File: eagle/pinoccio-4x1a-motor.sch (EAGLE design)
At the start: 27 parts, among them IC1 74LVC1G04DBV, IC2 74LVC1G04DBV, IC3 74LVC1G04DBV, IC4 74LVC1G04DBV, J1 POWER_JACKPTH, U1 TB6621FNG, U2 TB6621FNG

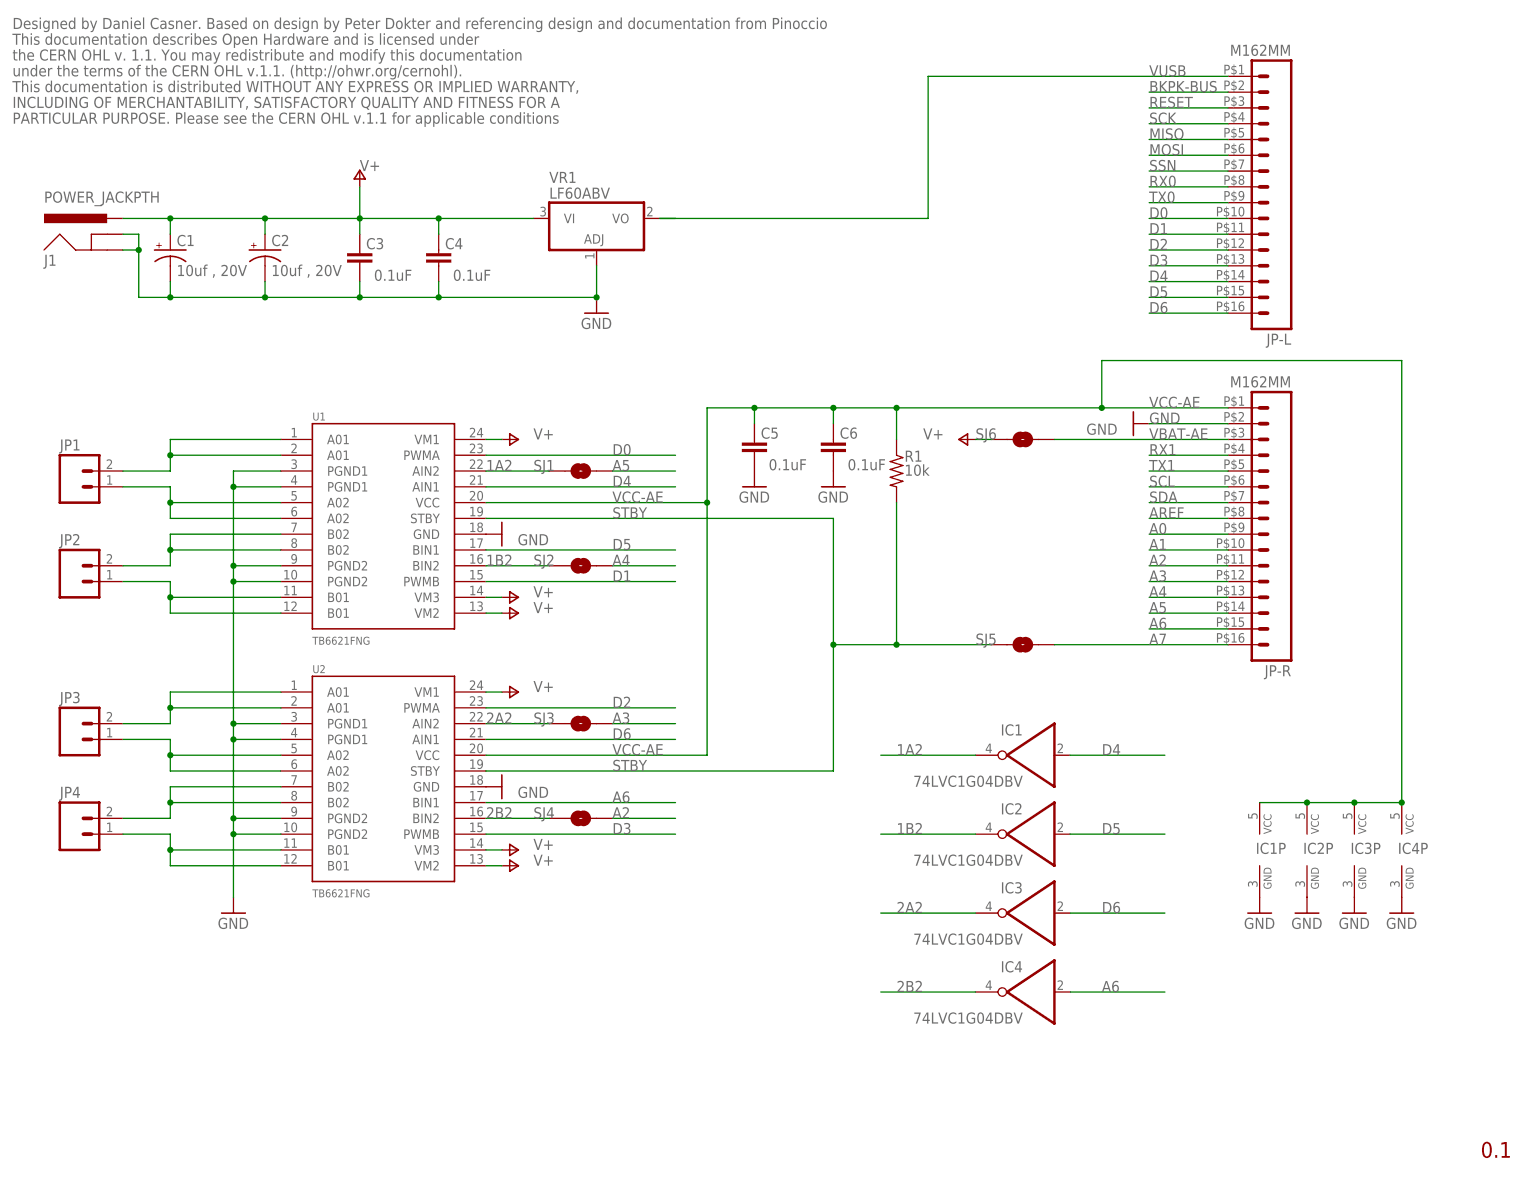
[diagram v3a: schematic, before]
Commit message: Add Atiny13 backpack ID chip. Connect LED and backpack standby to unused GPIO pins on the ATiny13.
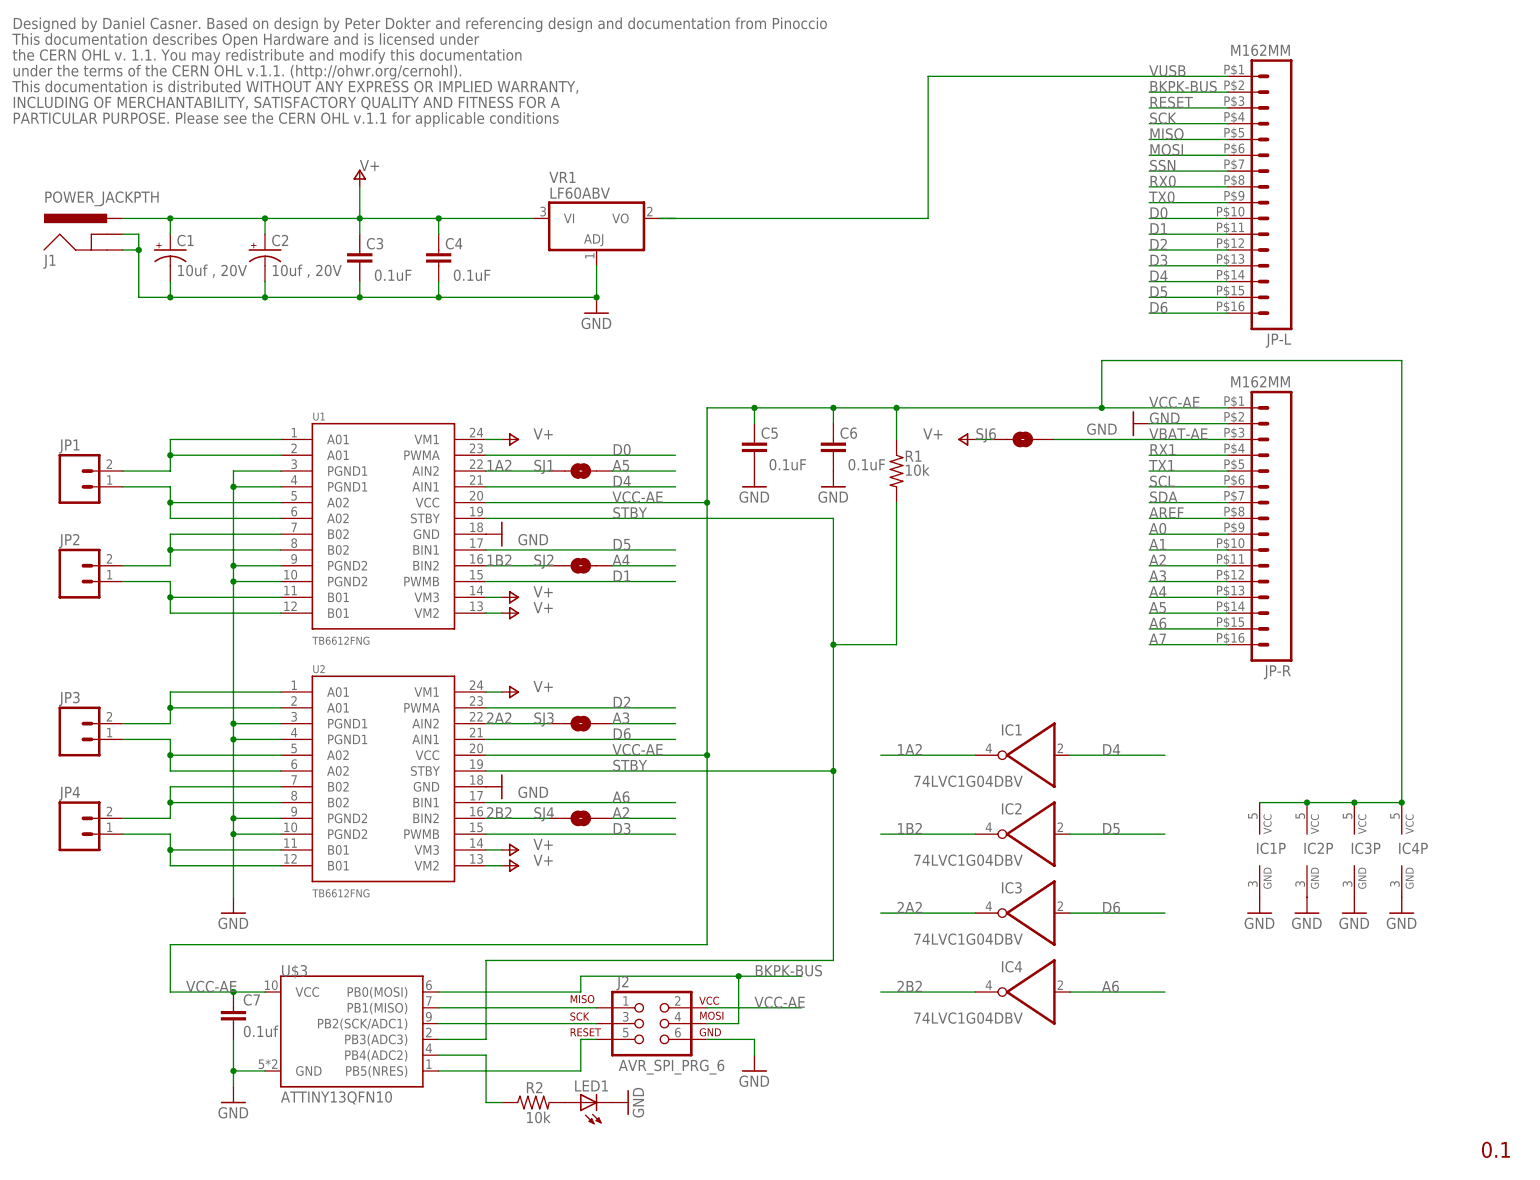
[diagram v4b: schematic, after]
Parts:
- removed SJ5: SOLDERJUMPERNC2, SparkFun-Passives:SOLDERJUMPERNC2
- added C7: 0.1uf, Pinoccio:CAP0402-CAP
- added J2: AVR_SPI_PRG_6, Pinoccio:AVR_SPI_PRG_6
- added LED1: (no value), SparkFun-LED:LED0603
- added R2: 10k, rcl:R-US_R0402
- added U$3: ATTINY13QFN10, Pinoccio:ATTINY13QFN10
- U1, U2: value TB6621FNG -> TB6612FNG
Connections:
- new net N$1: R2.1, U$3.PB4(ADC2)
- new net N$2: J2.1, U$3.PB1(MISO)
- new net N$3: J2.3, U$3.PB2(SCK/ADC1)
- new net N$4: J2.5, U$3.PB5(NRES)
- new net N$5: LED1.A, R2.2
- net A7: no longer SJ5.2
- net BKPK-BUS: now also J2.4, U$3.PB0(MOSI)
- net GND: now also C7.2, J2.6, LED1.C, U$3.GND
- net STBY: now also U$3.PB3(ADC3); no longer SJ5.1
- net VCC-AE: now also C7.1, J2.2, U$3.VCC
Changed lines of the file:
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@@
 <part name="JP-R" library="Pinoccio" deviceset="M16" device="2MM"/>
 <part name="JP-L" library="Pinoccio" deviceset="M16" device="2MM"/>
-<part name="U1" library="SparkFun" deviceset="TB6621FNG" device=""/>
-<part name="U2" library="SparkFun" deviceset="TB6621FNG" device=""/>
+<part name="U1" library="SparkFun" deviceset="TB6621FNG" device="" value="TB6612FNG"/>
+<part name="U2" library="SparkFun" deviceset="TB6621FNG" device="" value="TB6612FNG"/>
 <part name="VR1" library="linear" deviceset="*317" device="T" value="LF60ABV"/>
 <part name="C3" library="SparkFun" deviceset="CAP" device="0402-CAP" value="0.1uF"/>
@@
 <part name="P+7" library="supply1" deviceset="V+" device=""/>
 <part name="R1" library="rcl" deviceset="R-US_" device="R0402" value="10k"/>
-<part name="SJ5" library="SparkFun-Passives" deviceset="SOLDERJUMPER" device="NC2"/>
 <part name="SJ6" library="SparkFun-Passives" deviceset="SOLDERJUMPER" device="NC2"/>
 <part name="P+8" library="supply1" deviceset="V+" device=""/>
@@
 <part name="GND11" library="SparkFun-Aesthetics" deviceset="GND" device=""/>
 <part name="GND12" library="SparkFun-Aesthetics" deviceset="GND" device=""/>
+<part name="U$3" library="Pinoccio" deviceset="ATTINY13" device="QFN10"/>
+<part name="J2" library="Pinoccio" deviceset="AVR_SPI_PRG_6" device=""/>
+<part name="C7" library="Pinoccio" deviceset="CAP" device="0402-CAP" value="0.1uf"/>
+<part name="GND2" library="SparkFun-Aesthetics" deviceset="GND" device=""/>
+<part name="GND13" library="SparkFun-Aesthetics" deviceset="GND" device=""/>
+<part name="R2" library="rcl" deviceset="R-US_" device="R0402" value="10k"/>
+<part name="LED1" library="SparkFun-LED" deviceset="LED" device="0603"/>
+<part name="GND14" library="SparkFun-Aesthetics" deviceset="GND" device=""/>
 </parts>
 <sheets>
@@
 <attribute name="VALUE" x="146.05" y="110.998" size="1.778" layer="96"/>
 </instance>
-<instance part="SJ5" gate="1" x="165.1" y="83.82" smashed="yes">
-<attribute name="NAME" x="157.48" y="83.82" size="1.778" layer="95"/>
-</instance>
 <instance part="SJ6" gate="1" x="165.1" y="116.84" smashed="yes">
 <attribute name="NAME" x="157.48" y="116.84" size="1.778" layer="95"/>
@@
 <instance part="GND11" gate="1" x="134.62" y="109.22"/>
 <instance part="GND12" gate="1" x="121.92" y="109.22"/>
+<instance part="U$3" gate="G$1" x="58.42" y="20.32"/>
+<instance part="J2" gate="G$1" x="104.14" y="22.86"/>
+<instance part="C7" gate="G$1" x="38.1" y="22.86"/>
+<instance part="GND2" gate="1" x="38.1" y="10.16"/>
+<instance part="GND13" gate="1" x="121.92" y="15.24"/>
+<instance part="R2" gate="G$1" x="86.36" y="10.16" smashed="yes">
+<attribute name="NAME" x="85.09" y="11.6586" size="1.778" layer="95"/>
+<attribute name="VALUE" x="85.09" y="6.858" size="1.778" layer="96"/>
+</instance>
+<instance part="LED1" gate="G$1" x="93.98" y="10.16" rot="R90"/>
+<instance part="GND14" gate="1" x="101.6" y="10.16" rot="R90"/>
 </instances>
 <busses>
@@
 <pinref part="GND12" gate="1" pin="GND"/>
 </segment>
+<segment>
+<pinref part="U$3" gate="G$1" pin="GND"/>
+<wire x1="43.18" y1="15.24" x2="38.1" y2="15.24" width="0.1524" layer="91"/>
+<wire x1="38.1" y1="15.24" x2="38.1" y2="12.7" width="0.1524" layer="91"/>
+<pinref part="C7" gate="G$1" pin="2"/>
+<wire x1="38.1" y1="20.32" x2="38.1" y2="15.24" width="0.1524" layer="91"/>
+<junction x="38.1" y="15.24"/>
+<pinref part="GND2" gate="1" pin="GND"/>
+</segment>
+<segment>
+<pinref part="J2" gate="G$1" pin="6"/>
+<wire x1="114.3" y1="20.32" x2="121.92" y2="20.32" width="0.1524" layer="91"/>
+<wire x1="121.92" y1="20.32" x2="121.92" y2="17.78" width="0.1524" layer="91"/>
+<pinref part="GND13" gate="1" pin="GND"/>
+</segment>
+<segment>
+<pinref part="LED1" gate="G$1" pin="C"/>
+<pinref part="GND14" gate="1" pin="GND"/>
+</segment>
 </net>
 <net name="MOSI" class="0">
@@
 </segment>
 </net>
-<net name="A7" class="0">
-<segment>
-<pinref part="JP-R" gate="G$1" pin="16"/>
-<label x="185.42" y="83.82" size="1.778" layer="95"/>
-<wire x1="198.12" y1="83.82" x2="170.18" y2="83.82" width="0.1524" layer="91"/>
-<pinref part="SJ5" gate="1" pin="2"/>
-</segment>
-</net>
 <net name="VCC-AE" class="0">
 <segment>
@@
 <junction x="134.62" y="121.92"/>
 <junction x="121.92" y="121.92"/>
+<wire x1="114.3" y1="66.04" x2="114.3" y2="35.56" width="0.1524" layer="91"/>
+<pinref part="U$3" gate="G$1" pin="VCC"/>
+<wire x1="43.18" y1="27.94" x2="38.1" y2="27.94" width="0.1524" layer="91"/>
+<label x="30.48" y="27.94" size="1.778" layer="95"/>
+<pinref part="C7" gate="G$1" pin="1"/>
+<wire x1="38.1" y1="27.94" x2="27.94" y2="27.94" width="0.1524" layer="91"/>
+<junction x="38.1" y="27.94"/>
+<wire x1="114.3" y1="35.56" x2="27.94" y2="35.56" width="0.1524" layer="91"/>
+<wire x1="27.94" y1="35.56" x2="27.94" y2="27.94" width="0.1524" layer="91"/>
+<junction x="114.3" y="66.04"/>
+</segment>
+<segment>
+<pinref part="J2" gate="G$1" pin="2"/>
+<wire x1="114.3" y1="25.4" x2="129.54" y2="25.4" width="0.1524" layer="91"/>
+<label x="121.92" y="25.4" size="1.778" layer="95"/>
 </segment>
 </net>
@@
 <label x="99.06" y="104.14" size="1.778" layer="95"/>
 <pinref part="R1" gate="G$1" pin="2"/>
-<pinref part="SJ5" gate="1" pin="1"/>
 <wire x1="144.78" y1="106.68" x2="144.78" y2="83.82" width="0.1524" layer="91"/>
-<wire x1="144.78" y1="83.82" x2="160.02" y2="83.82" width="0.1524" layer="91"/>
 <wire x1="144.78" y1="83.82" x2="134.62" y2="83.82" width="0.1524" layer="91"/>
 <wire x1="134.62" y1="104.14" x2="134.62" y2="83.82" width="0.1524" layer="91"/>
@@
 <wire x1="134.62" y1="83.82" x2="134.62" y2="63.5" width="0.1524" layer="91"/>
 <junction x="134.62" y="83.82"/>
-<junction x="144.78" y="83.82"/>
+<wire x1="78.74" y1="33.02" x2="134.62" y2="33.02" width="0.1524" layer="91"/>
+<wire x1="134.62" y1="33.02" x2="134.62" y2="63.5" width="0.1524" layer="91"/>
+<junction x="134.62" y="63.5"/>
+<wire x1="78.74" y1="33.02" x2="78.74" y2="20.32" width="0.1524" layer="91"/>
+<pinref part="U$3" gate="G$1" pin="PB3(ADC3)"/>
+<wire x1="78.74" y1="20.32" x2="71.12" y2="20.32" width="0.1524" layer="91"/>
 </segment>
 </net>
@@
 <wire x1="198.12" y1="172.72" x2="185.42" y2="172.72" width="0.1524" layer="91"/>
 </segment>
+<segment>
+<pinref part="J2" gate="G$1" pin="4"/>
+<wire x1="114.3" y1="22.86" x2="119.38" y2="22.86" width="0.1524" layer="91"/>
+<wire x1="119.38" y1="22.86" x2="119.38" y2="30.48" width="0.1524" layer="91"/>
+<pinref part="U$3" gate="G$1" pin="PB0(MOSI)"/>
+<wire x1="119.38" y1="30.48" x2="93.98" y2="30.48" width="0.1524" layer="91"/>
+<wire x1="93.98" y1="30.48" x2="93.98" y2="27.94" width="0.1524" layer="91"/>
+<wire x1="93.98" y1="27.94" x2="71.12" y2="27.94" width="0.1524" layer="91"/>
+<wire x1="119.38" y1="30.48" x2="129.54" y2="30.48" width="0.1524" layer="91"/>
+<junction x="119.38" y="30.48"/>
+<label x="121.92" y="30.48" size="1.778" layer="95"/>
+</segment>
+</net>
+<net name="N$3" class="0">
+<segment>
+<pinref part="J2" gate="G$1" pin="3"/>
+<pinref part="U$3" gate="G$1" pin="PB2(SCK/ADC1)"/>
+<wire x1="96.52" y1="22.86" x2="71.12" y2="22.86" width="0.1524" layer="91"/>
+</segment>
+</net>
+<net name="N$4" class="0">
+<segment>
+<pinref part="J2" gate="G$1" pin="5"/>
+<wire x1="96.52" y1="20.32" x2="93.98" y2="20.32" width="0.1524" layer="91"/>
+<wire x1="93.98" y1="20.32" x2="93.98" y2="15.24" width="0.1524" layer="91"/>
+<pinref part="U$3" gate="G$1" pin="PB5(NRES)"/>
+<wire x1="93.98" y1="15.24" x2="71.12" y2="15.24" width="0.1524" layer="91"/>
+</segment>
+</net>
+<net name="A7" class="0">
+<segment>
+<pinref part="JP-R" gate="G$1" pin="16"/>
+<wire x1="198.12" y1="83.82" x2="185.42" y2="83.82" width="0.1524" layer="91"/>
+<label x="185.42" y="83.82" size="1.778" layer="95"/>
+</segment>
+</net>
+<net name="N$1" class="0">
+<segment>
+<pinref part="U$3" gate="G$1" pin="PB4(ADC2)"/>
+<pinref part="R2" gate="G$1" pin="1"/>
+<wire x1="81.28" y1="10.16" x2="78.74" y2="10.16" width="0.1524" layer="91"/>
+<wire x1="78.74" y1="10.16" x2="78.74" y2="17.78" width="0.1524" layer="91"/>
+<wire x1="78.74" y1="17.78" x2="71.12" y2="17.78" width="0.1524" layer="91"/>
+</segment>
+</net>
+<net name="N$2" class="0">
+<segment>
+<pinref part="U$3" gate="G$1" pin="PB1(MISO)"/>
+<pinref part="J2" gate="G$1" pin="1"/>
+<wire x1="96.52" y1="25.4" x2="71.12" y2="25.4" width="0.1524" layer="91"/>
+</segment>
+</net>
+<net name="N$5" class="0">
+<segment>
+<pinref part="R2" gate="G$1" pin="2"/>
+<pinref part="LED1" gate="G$1" pin="A"/>
+</segment>
 </net>

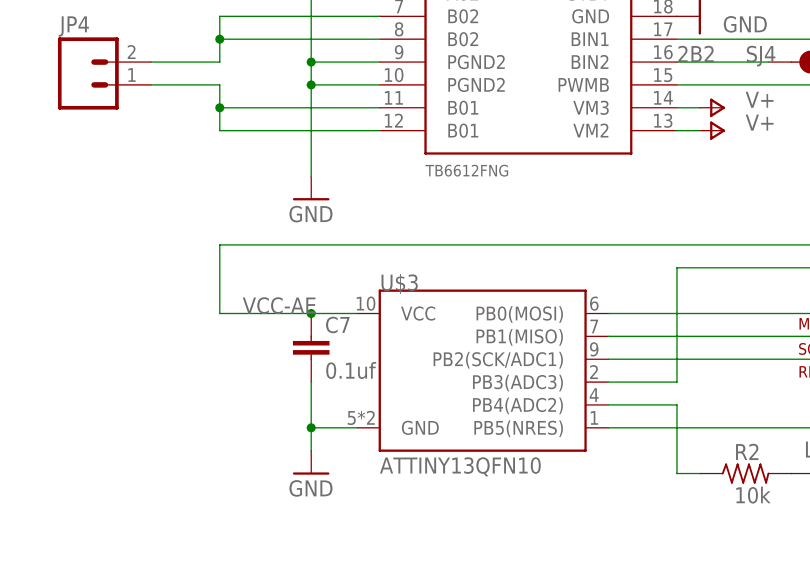
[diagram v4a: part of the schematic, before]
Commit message: Tru ripping up all the autorouted signals before rerouting.
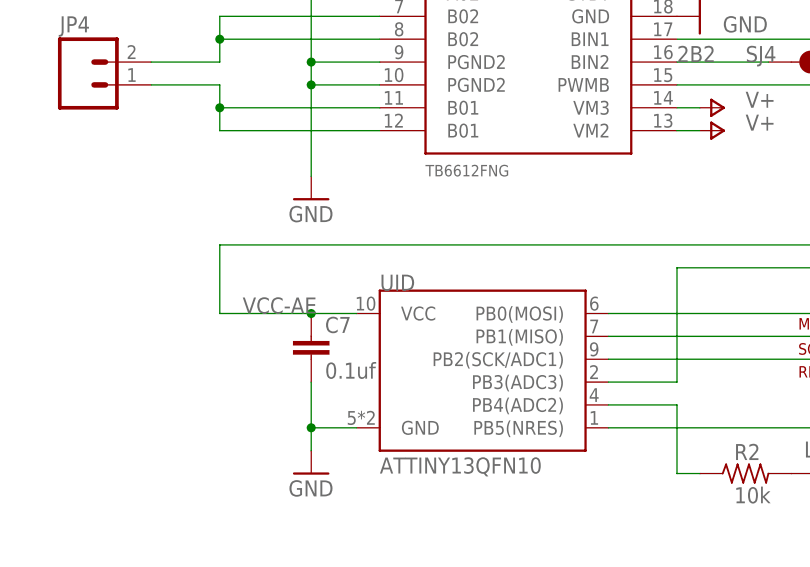
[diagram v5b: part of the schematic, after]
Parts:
- renumbered U$3 to UID
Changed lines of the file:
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@@
 <part name="GND11" library="SparkFun-Aesthetics" deviceset="GND" device=""/>
 <part name="GND12" library="SparkFun-Aesthetics" deviceset="GND" device=""/>
-<part name="U$3" library="Pinoccio" deviceset="ATTINY13" device="QFN10"/>
+<part name="UID" library="Pinoccio" deviceset="ATTINY13" device="QFN10"/>
 <part name="J2" library="Pinoccio" deviceset="AVR_SPI_PRG_6" device=""/>
 <part name="C7" library="Pinoccio" deviceset="CAP" device="0402-CAP" value="0.1uf"/>
@@
 <instance part="GND11" gate="1" x="134.62" y="109.22"/>
 <instance part="GND12" gate="1" x="121.92" y="109.22"/>
-<instance part="U$3" gate="G$1" x="58.42" y="20.32"/>
+<instance part="UID" gate="G$1" x="58.42" y="20.32"/>
 <instance part="J2" gate="G$1" x="104.14" y="22.86"/>
 <instance part="C7" gate="G$1" x="38.1" y="22.86"/>
@@
 </segment>
 <segment>
-<pinref part="U$3" gate="G$1" pin="GND"/>
+<pinref part="UID" gate="G$1" pin="GND"/>
 <wire x1="43.18" y1="15.24" x2="38.1" y2="15.24" width="0.1524" layer="91"/>
 <wire x1="38.1" y1="15.24" x2="38.1" y2="12.7" width="0.1524" layer="91"/>
@@
 <junction x="121.92" y="121.92"/>
 <wire x1="114.3" y1="66.04" x2="114.3" y2="35.56" width="0.1524" layer="91"/>
-<pinref part="U$3" gate="G$1" pin="VCC"/>
+<pinref part="UID" gate="G$1" pin="VCC"/>
 <wire x1="43.18" y1="27.94" x2="38.1" y2="27.94" width="0.1524" layer="91"/>
 <label x="30.48" y="27.94" size="1.778" layer="95"/>
@@
 <junction x="134.62" y="63.5"/>
 <wire x1="78.74" y1="33.02" x2="78.74" y2="20.32" width="0.1524" layer="91"/>
-<pinref part="U$3" gate="G$1" pin="PB3(ADC3)"/>
+<pinref part="UID" gate="G$1" pin="PB3(ADC3)"/>
 <wire x1="78.74" y1="20.32" x2="71.12" y2="20.32" width="0.1524" layer="91"/>
 </segment>
@@
 <wire x1="114.3" y1="22.86" x2="119.38" y2="22.86" width="0.1524" layer="91"/>
 <wire x1="119.38" y1="22.86" x2="119.38" y2="30.48" width="0.1524" layer="91"/>
-<pinref part="U$3" gate="G$1" pin="PB0(MOSI)"/>
+<pinref part="UID" gate="G$1" pin="PB0(MOSI)"/>
 <wire x1="119.38" y1="30.48" x2="93.98" y2="30.48" width="0.1524" layer="91"/>
 <wire x1="93.98" y1="30.48" x2="93.98" y2="27.94" width="0.1524" layer="91"/>
@@
 <segment>
 <pinref part="J2" gate="G$1" pin="3"/>
-<pinref part="U$3" gate="G$1" pin="PB2(SCK/ADC1)"/>
+<pinref part="UID" gate="G$1" pin="PB2(SCK/ADC1)"/>
 <wire x1="96.52" y1="22.86" x2="71.12" y2="22.86" width="0.1524" layer="91"/>
 </segment>
@@
 <wire x1="96.52" y1="20.32" x2="93.98" y2="20.32" width="0.1524" layer="91"/>
 <wire x1="93.98" y1="20.32" x2="93.98" y2="15.24" width="0.1524" layer="91"/>
-<pinref part="U$3" gate="G$1" pin="PB5(NRES)"/>
+<pinref part="UID" gate="G$1" pin="PB5(NRES)"/>
 <wire x1="93.98" y1="15.24" x2="71.12" y2="15.24" width="0.1524" layer="91"/>
 </segment>
@@
 <net name="N$1" class="0">
 <segment>
-<pinref part="U$3" gate="G$1" pin="PB4(ADC2)"/>
+<pinref part="UID" gate="G$1" pin="PB4(ADC2)"/>
 <pinref part="R2" gate="G$1" pin="1"/>
 <wire x1="81.28" y1="10.16" x2="78.74" y2="10.16" width="0.1524" layer="91"/>
@@
 <net name="N$2" class="0">
 <segment>
-<pinref part="U$3" gate="G$1" pin="PB1(MISO)"/>
+<pinref part="UID" gate="G$1" pin="PB1(MISO)"/>
 <pinref part="J2" gate="G$1" pin="1"/>
 <wire x1="96.52" y1="25.4" x2="71.12" y2="25.4" width="0.1524" layer="91"/>
